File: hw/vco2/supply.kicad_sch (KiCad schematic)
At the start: 22 parts, among them J1 Conn_02x08_Odd_Even, Q1 DNP, U2 TL431BCDBZ, U3 TL072HxD, U6 TL431BCDBV

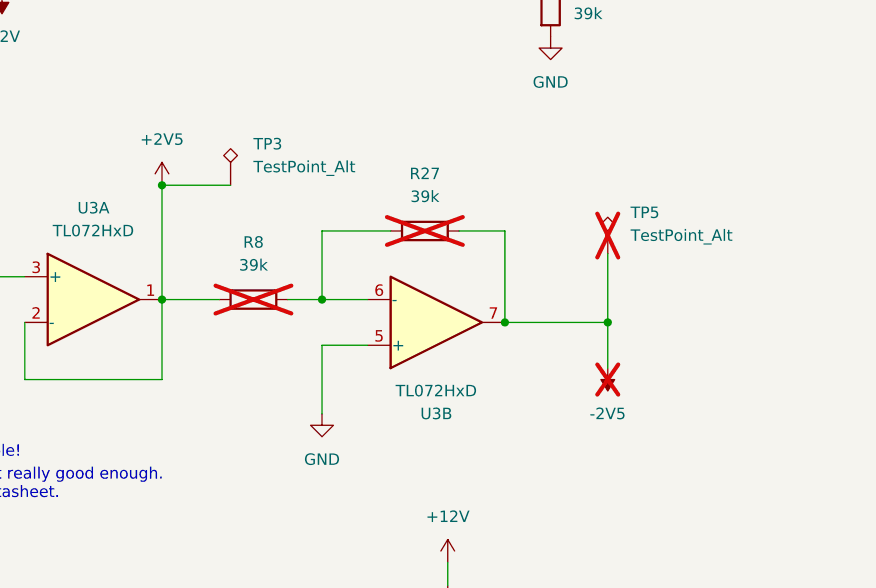
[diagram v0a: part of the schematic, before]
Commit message: Layout VCO2 board
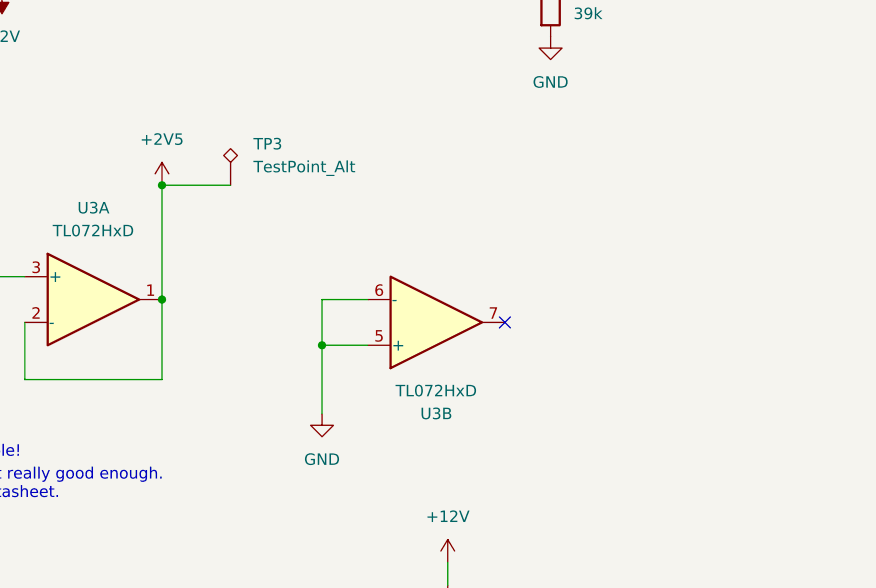
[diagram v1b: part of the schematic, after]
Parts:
- removed R27, R8: 39k, Resistor_SMD:R_0603_1608Metric_Pad0.98x0.95mm_HandSolder, symbol Device:R
- removed TP5: TestPoint_Alt, Holes:TP_0.9mm, symbol Connector:TestPoint_Alt
- J1: footprint Connector_IDC:IDC-Header_2x08_P2.54mm_Vertical -> Eurorack:IDC-Header_2x08_P2.54mm_Vertical
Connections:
- net GND: now also U3.6 (-)
- net -2V5: no longer names the net of U3.7
- no-connect marks 0 -> 1

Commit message: Place components
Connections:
- no-connect marks 1 -> 4
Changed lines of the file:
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@@
 		(at 229.87 105.41)
+	)
+	(no_connect
+		(at 50.8 111.76)
+	)
+	(no_connect
+		(at 38.1 109.22)
+	)
+	(no_connect
+		(at 38.1 111.76)
 	)
 	(wire

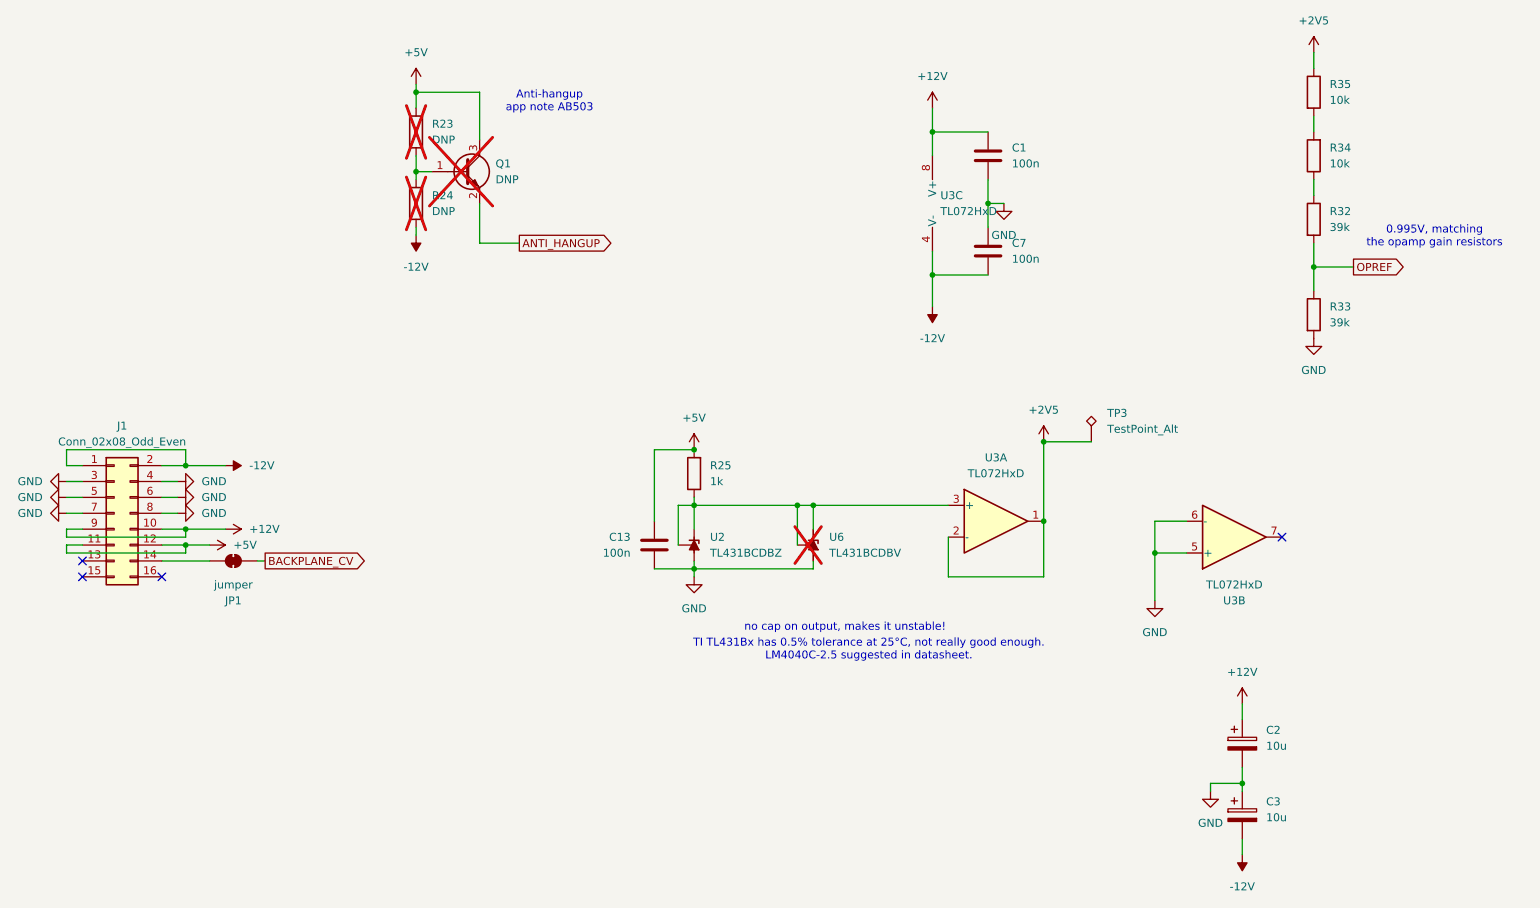
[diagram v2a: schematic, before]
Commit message: WIP: Redesign VCO2 board
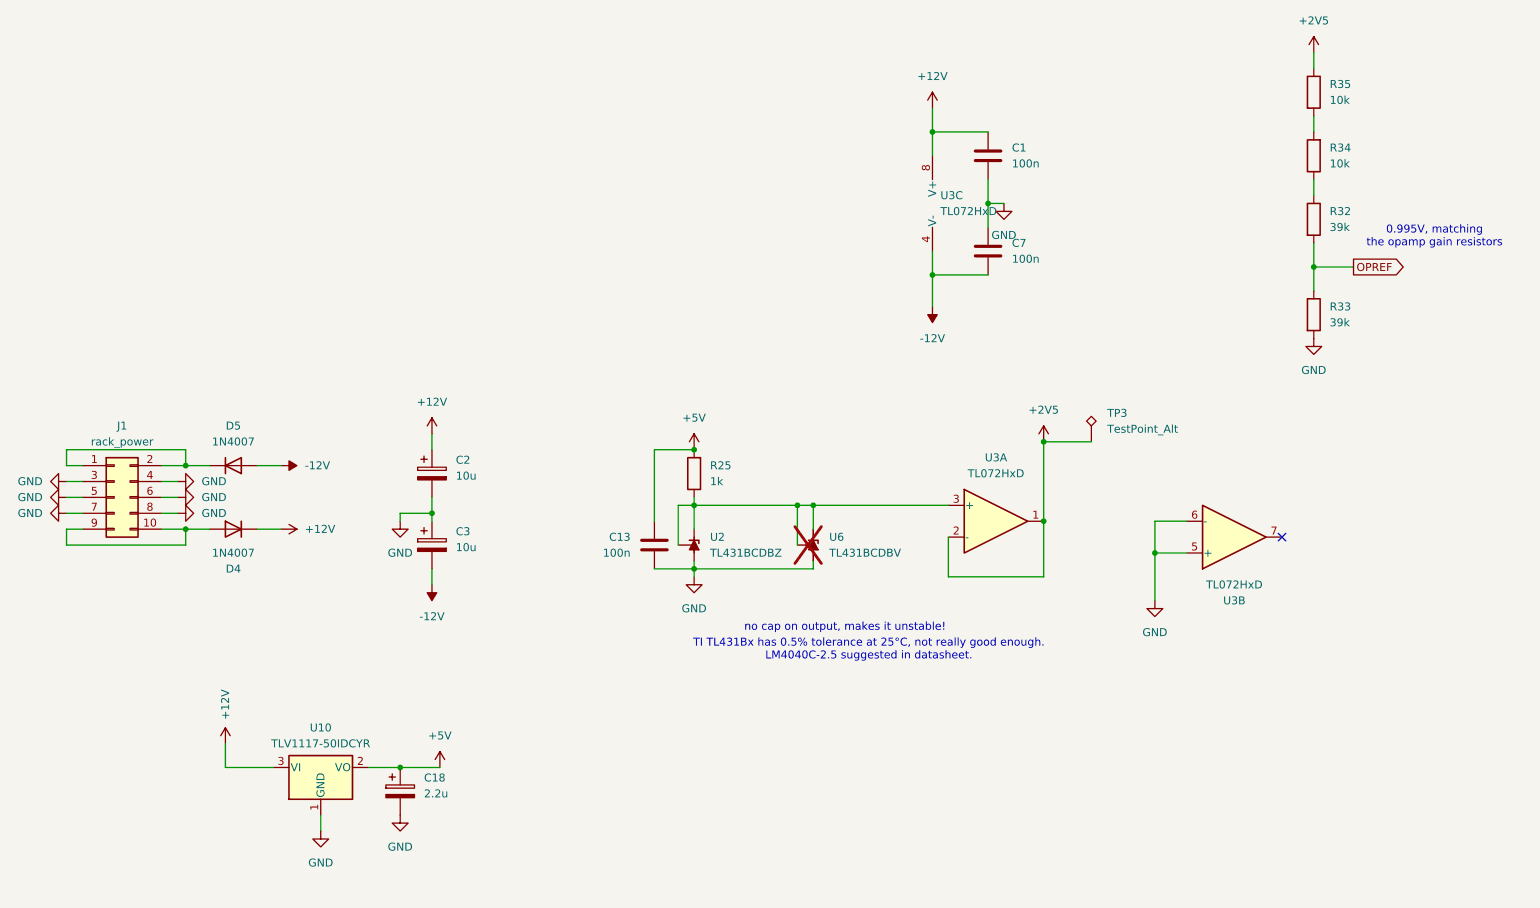
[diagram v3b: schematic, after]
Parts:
- removed J1: Conn_02x08_Odd_Even, Eurorack:IDC-Header_2x08_P2.54mm_Vertical, symbol Connector_Generic:Conn_02x08_Odd_Even
- removed JP1: jumper, Jumper:SolderJumper-2_P1.3mm_Bridged2Bar_Pad1.0x1.5mm, symbol Jumper:SolderJumper_2_Bridged
- removed Q1: DNP, Package_TO_SOT_SMD:SOT-23, symbol Transistor_BJT:BC847
- removed R23, R24: DNP, Resistor_SMD:R_0603_1608Metric_Pad0.98x0.95mm_HandSolder, symbol Device:R
- added C18: 2.2u, Capacitor_SMD:C_0805_2012Metric, symbol Device:C_Polarized
- added D4, D5: 1N4007, Diode_SMD:D_SOD-323, symbol Diode:1N4148WT
- added J1: rack_power, Eurorack:IDC-Header_2x05_P2.54mm_Vertical, symbol Connector_Generic:Conn_02x05_Odd_Even
- added U10: TLV1117-50IDCYR, Package_TO_SOT_SMD:SOT-223-3_TabPin2, symbol Regulator_Linear:TLV1117-50
- C1, C13, C7: footprint Capacitor_SMD:C_0603_1608Metric_Pad1.08x0.95mm_HandSolder -> Capacitor_SMD:C_0603_1608Metric
- R25, R32, R33, R34, R35: footprint Resistor_SMD:R_0603_1608Metric_Pad0.98x0.95mm_HandSolder -> Resistor_SMD:R_0603_1608Metric
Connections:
- net +12V: now also D4.1 (K), U10.3 (VI)
- net +5V: now also C18.1, U10.2 (VO)
- net -12V: now also D5.2 (A)
- net GND: now also C18.2, J1.3 (Pin_3), J1.4 (Pin_4), J1.5 (Pin_5), J1.6 (Pin_6), J1.7 (Pin_7), J1.8 (Pin_8), U10.1 (GND)
- new net: D5.1 (K), J1.1 (Pin_1), J1.2 (Pin_2)
- new net: D4.2 (A), J1.10 (Pin_10), J1.9 (Pin_9)
- no-connect marks 4 -> 1
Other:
- note removed: "Anti-hangup app note AB503"
- moved on the sheet: C2, C3

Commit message: VCO2 production work
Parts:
- U10: LCSC (none) -> C15512
- U2: LCSC (none) -> C6971
- U3: LCSC (none) -> C4370389
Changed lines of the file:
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@@
+			)
+		)
+		(property "LCSC" "C6971"
+			(at 135.89 106.68 90)
+			(effects
+				(font
+					(size 1.27 1.27)
+				)
+				(hide yes)
 			)
 		)
@@
 		)
 		(property "Description" "Dual Low-Noise JFET-Input Operational Amplifiers, DIP-8/SOIC-8"
+			(at 176.53 52.07 0)
+			(effects
+				(font
+					(size 1.27 1.27)
+				)
+				(hide yes)
+			)
+		)
+		(property "LCSC" "C4370389"
 			(at 176.53 52.07 0)
 			(effects
@@
 			)
 		)
+		(property "LCSC" "C4370389"
+			(at 222.25 105.41 0)
+			(effects
+				(font
+					(size 1.27 1.27)
+				)
+				(hide yes)
+			)
+		)
 		(pin "1"
 		)
@@
 			)
 		)
+		(property "LCSC" "C4370389"
+			(at 184.15 102.87 0)
+			(effects
+				(font
+					(size 1.27 1.27)
+				)
+				(hide yes)
+			)
+		)
 		(pin "1"
 		)
@@
 			(at 76.2 142.24 0)
 			(effects
+				(font
+					(size 1.27 1.27)
+				)
+				(hide yes)
+			)
+		)
+		(property "LCSC" "C15512"
+			(at 76.2 142.24 0)
+			(effects

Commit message: VCO2 rev 2 as sent for production at JLCPCB
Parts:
- D4, D5: LCSC (none) -> C2128
- U10: LCSC C15512 -> C6187
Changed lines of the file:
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@@
+			)
+		)
+		(property "LCSC" "C2128"
+			(at 62.23 93.98 0)
+			(effects
+				(font
+					(size 1.27 1.27)
+				)
+				(hide yes)
 			)
 		)
@@
 			)
 		)
+		(property "LCSC" "C2128"
+			(at 62.23 104.14 0)
+			(effects
+				(font
+					(size 1.27 1.27)
+				)
+				(hide yes)
+			)
+		)
 		(pin "1"
 		)
@@
 			)
 		)
-		(property "LCSC" "C15512"
+		(property "LCSC" "C6187"
 			(at 76.2 142.24 0)
 			(effects
